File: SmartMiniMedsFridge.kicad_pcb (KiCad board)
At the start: 2 copper layers, 138 x 40 mm, 48 parts, among them J1 USB_C_Receptacle_USB2.0, J2 XHB-6AW, J3 Qwiic I2C, J4 Stemma I2C, U1 AMS1117-3.3, U2 ESP32-S3-WROOM-1, U3 LMV321, U4 MPR121QR2, U5 SSD1306

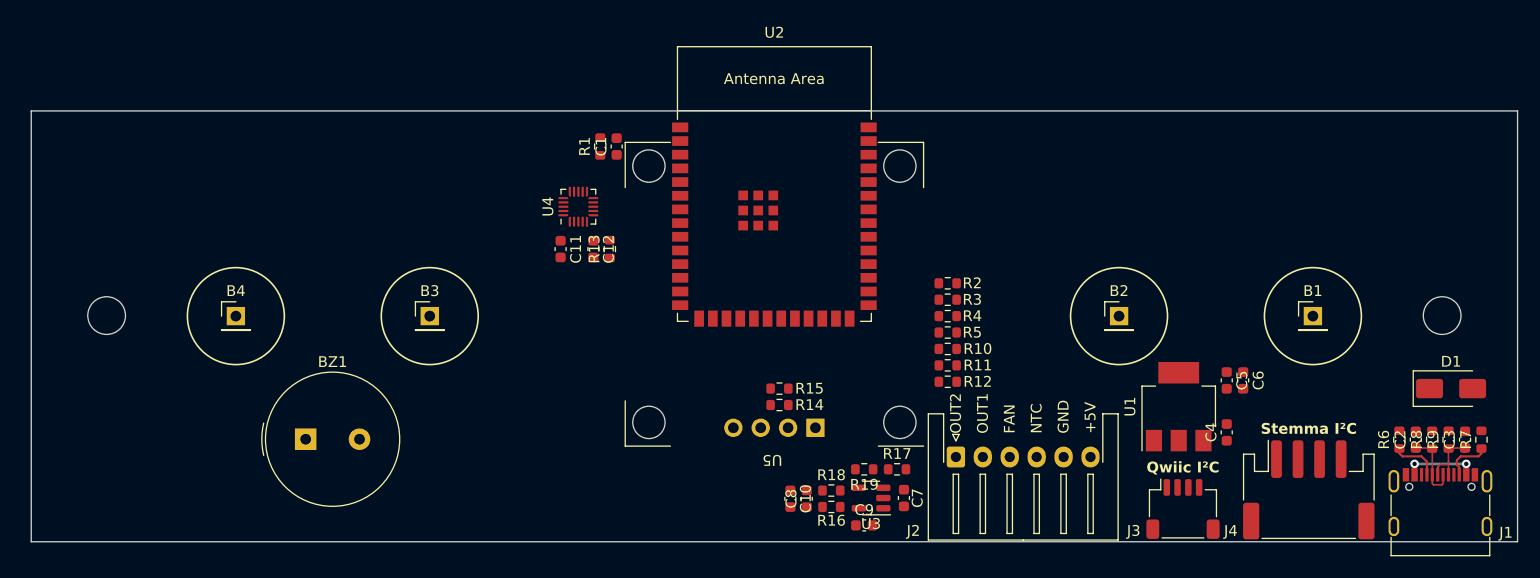
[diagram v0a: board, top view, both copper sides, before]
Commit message: pre re-arrangement because of collision with case
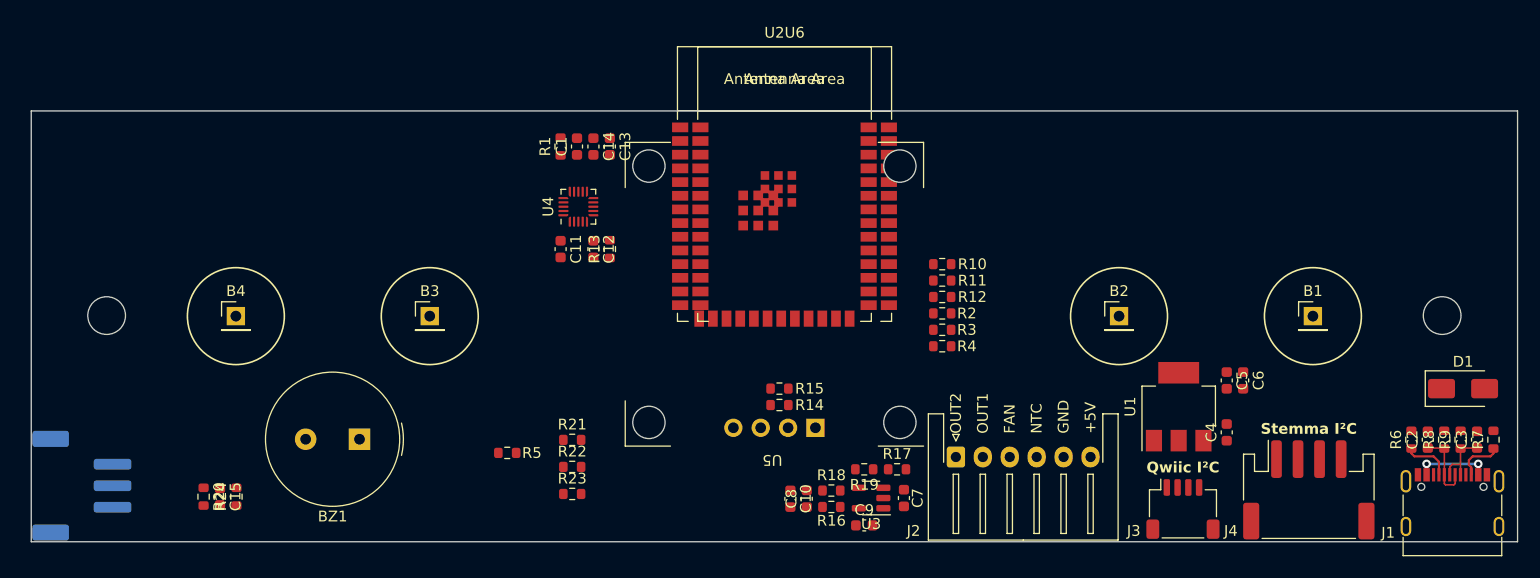
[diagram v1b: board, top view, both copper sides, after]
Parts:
- added C13: 22uF, Capacitor_SMD:C_0603_1608Metric, F.Cu at (117.2, 79.5)
- added C14: 100nF, Capacitor_SMD:C_0603_1608Metric, F.Cu at (115.7, 79.5)
- added C15: 100nF, Capacitor_SMD:C_0603_1608Metric, F.Cu at (81.0, 112.0)
- added J5: Door Sensor, Connector_JST:JST_PH_S3B-PH-SM4-TB_1x03-1MP_P2.00mm_Horizontal, B.Cu at (68.2, 111.0)
- added R20: 10k, Resistor_SMD:R_0603_1608Metric, F.Cu at (79.5, 112.0)
- added R21: 0R, Resistor_SMD:R_0603_1608Metric, F.Cu at (113.7, 106.7)
- added R22: 0R, Resistor_SMD:R_0603_1608Metric, F.Cu at (113.7, 109.2)
- added R23: 10k, Resistor_SMD:R_0603_1608Metric, F.Cu at (113.7, 111.8)
- added R24: 10k, Resistor_SMD:R_0603_1608Metric, F.Cu at (82.5, 112.0)
- added U6: ESP32-C6-WROOM-1, Espressif:ESP32-C6-WROOM-1, F.Cu at (134.4, 86.0)
- B1, B2, B3, B4: value Conn_01x01 -> Spring Contact
- U2: footprint PCM_Espressif:ESP32-S3-WROOM-1 -> Espressif:ESP32-S3-WROOM-1
- moved R5 42.4 mm to (107.7, 108.0)
- moved R11 7.89 mm to (148.1, 91.9)
- moved R12 7.89 mm to (148.1, 93.5)
- moved R10 7.89 mm to (148.1, 90.4)
- moved BZ1 5.00 mm to (94.0, 106.7), turned to 180 degrees
- moved C1 3.68 mm to (114.2, 79.5)
- moved R1 3.68 mm to (112.6, 79.5)
- moved R2 2.84 mm to (148.1, 95.0)
- moved R3 2.84 mm to (148.1, 96.5)
- moved R4 2.84 mm to (148.1, 98.0)
- moved C2 1.12 mm to (193.2, 106.7)
- moved C3 1.12 mm to (197.7, 106.7)
- moved D1 1.12 mm to (196.4, 102.0)
- moved J1 1.12 mm to (195.5, 113.7)
- moved R6 1.12 mm to (191.6, 106.7)
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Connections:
- J3 pad 3: SDA -> Ext_SDA
- J3 pad 4: SCL -> Ext_SCL
- J3 pad MP: (no net) -> unconnected-(J3-MountPin-PadMP)
- J4 pad 1: SCL -> Ext_SCL
- J4 pad 2: SDA -> Ext_SDA
- J4 pad MP: (no net) -> unconnected-(J4-MountPin-PadMP)
- R4 pad 1: Buzzer -> GPIO46
- R5 pad 1: C6_GPIO9 -> +3V3
- R5 pad 2: +3V3 -> Ext_SDA
- U2 pad 10: unconnected-(U2-GPIO17/U1TXD/ADC2_CH6-Pad10) -> /~{Touch_INT}
- U2 pad 11: /~{Touch_INT} -> /Door
- U2 pad 12: unconnected-(U2-GPIO8/TOUCH8/ADC1_CH7/SUBSPICS1-Pad12) -> Buzzer
- U2 pad 15: C6_GPIO9 -> unconnected-(U2-GPIO3/TOUCH3/ADC1_CH2-Pad15)
- U2 pad 16: Buzzer -> GPIO46
- U2 pad 17: SDA -> unconnected-(U2-GPIO9/TOUCH9/ADC1_CH8/FSPIHD/SUBSPIHD-Pad17)
- U2 pad 18: SCL -> unconnected-(U2-GPIO10/TOUCH10/ADC1_CH9/FSPICS0/FSPIIO4/SUBSPICS0-Pad18)
- U2 pad 19: /FAN_CPU -> unconnected-(U2-GPIO11/TOUCH11/ADC2_CH0/FSPID/FSPIIO5/SUBSPID-Pad19)
- U2 pad 20: /OUT1_CPU -> unconnected-(U2-GPIO12/TOUCH12/ADC2_CH1/FSPICLK/FSPIIO6/SUBSPICLK-Pad20)
- U2 pad 21: /OUT2_CPU -> unconnected-(U2-GPIO13/TOUCH13/ADC2_CH2/FSPIQ/FSPIIO7/SUBSPIQ-Pad21)
- U2 pad 28: unconnected-(U2-SPIIO6/GPIO35/FSPID/SUBSPID-Pad28) -> /OUT2_CPU
- U2 pad 29: unconnected-(U2-SPIIO7/GPIO36/FSPICLK/SUBSPICLK-Pad29) -> /OUT1_CPU
- U2 pad 30: unconnected-(U2-SPIDQS/GPIO37/FSPIQ/SUBSPIQ-Pad30) -> /FAN_CPU
- U2 pad 8: unconnected-(U2-GPIO15/U0RTS/ADC2_CH4/XTAL_32K_P-Pad8) -> SCL
- U2 pad 9: unconnected-(U2-GPIO16/U0CTS/ADC2_CH5/XTAL_32K_N-Pad9) -> SDA

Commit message: 1st production version
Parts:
- removed the U6 at (134.4, 86.0)
- added D2: LED_Small, LED_SMD:LED_0603_1608Metric, F.Cu at (149.2, 94.2)
- added D3: LED_Small, LED_SMD:LED_0603_1608Metric, F.Cu at (178.1, 86.4)
- added J6: UART, Connector_PinHeader_2.54mm:PinHeader_1x06_P2.54mm_Vertical, F.Cu at (161.0, 80.9)
- added R18: 1k, Resistor_SMD:R_0603_1608Metric, F.Cu at (144.0, 88.9)
- added R19: 1k, Resistor_SMD:R_0603_1608Metric, F.Cu at (178.1, 83.3)
- added R24: 100R, Resistor_SMD:R_0603_1608Metric, F.Cu at (144.0, 96.5)
- added REF**: OSHW-Logo2_9.8x8mm_SilkScreen, Symbol:OSHW-Logo2_9.8x8mm_SilkScreen, F.Cu at (69.6, 88.0)
- added SW1: Reset, Button_Switch_SMD:SW_Push_1P1T-SH_NO_CK_KMR2xxG, F.Cu at (103.5, 79.5)
- J1: footprint Connector_USB:USB_C_Receptacle_G-Switch_GT-USB-7010ASV -> Connector_USB:USB_C_Receptacle_G-Switch_GT-USB-7051x
- J5: moved to F.Cu
- moved D1 93.4 mm to (103.6, 112.4), turned to -90 degrees
- moved C5 89.5 mm to (108.2, 107.7)
- moved R11 86.5 mm to (109.7, 107.7)
- moved J1 85.0 mm to (110.5, 112.4)
- moved R6 85.0 mm to (114.3, 107.7)
- moved R5 85.0 mm to (106.7, 107.7)
- moved R10 83.4 mm to (111.3, 107.7)
- moved C4 80.4 mm to (112.8, 107.7)
- moved R12 51.0 mm to (158.4, 102.6), turned to 180 degrees
- moved R13 45.3 mm to (158.4, 104.1), turned to 180 degrees
- moved R15 41.9 mm to (155.3, 104.1)
- moved R14 41.8 mm to (155.3, 102.6)
- moved R16 30.6 mm to (153.8, 86.9)
- moved C10 29.3 mm to (151.5, 87.7)
- moved C11 29.3 mm to (156.8, 90.2)
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- renumbered C13 to C1, C8 to C10, C9 to C11, C15 to C12, C10 to C13, C11 to C14, C12 to C15, C14 to C2, C1 to C3, C2 to C4, C3 to C5, C7 to C6, C4 to C7, C5 to C8, C6 to C9, R2 to R1, R8 to R10, R9 to R11, R5 to R12, R23 to R13, R21 to R14, R22 to R15, R18 to R17, R3 to R2, R17 to R21, R24 to R22, R19 to R23, R14 to R25, R15 to R26, R13 to R27, R4 to R3, R1 to R4, R6 to R5, R7 to R6, R10 to R7, R11 to R8, R12 to R9, U3 to U2, U2 to U3, U4 to U5, U5 to U6
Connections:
- J1 pad S1: unconnected-(J1-SHIELD-PadS1) -> GND
- J3 pad MP: unconnected-(J3-MountPin-PadMP) -> GND
- J4 pad MP: unconnected-(J4-MountPin-PadMP) -> GND
- J5 pad MP: unconnected-(J5-MountPin-PadMP) -> GND
- U3 pad 24: unconnected-(U2-GPIO47/SPICLK_P/SUBSPICLK_P_DIFF-Pad24) -> Ext_SDA
- U3 pad 25: unconnected-(U2-GPIO48/SPICLK_N/SUBSPICLK_N_DIFF-Pad25) -> Ext_SCL
- U3 pad 31: unconnected-(U2-GPIO38/FSPIWP/SUBSPIWP-Pad31) -> /GPIO38
- U3 pad 32: unconnected-(U2-MTCK/GPIO39/CLK_OUT3/SUBSPICS1-Pad32) -> /GPIO39
- U3 pad 33: unconnected-(U2-MTDO/GPIO40/CLK_OUT2-Pad33) -> /GPIO40
- U3 pad 35: unconnected-(U2-MTMS/GPIO42-Pad35) -> /GPIO42
- U3 pad 8: SCL -> SDA
- U3 pad 9: SDA -> SCL
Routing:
- net +3V3: track 0.00 -> 249.9 mm, vias 0 -> 7
- net +5V: track 0.00 -> 141.3 mm, vias 0 -> 5
- net Touch0: track 0.00 -> 86.9 mm, vias 0 -> 2
- net SDA: track 0.00 -> 74.9 mm, vias 0 -> 3
- net SCL: track 0.00 -> 73.4 mm, vias 0 -> 3
- net Touch1: track 0.00 -> 68.7 mm, vias 0 -> 2
- net ~{RESET}: track 0.00 -> 67.9 mm, vias 0 -> 4
- net Touch3: track 0.00 -> 54.2 mm, vias 0 -> 1
- net /Door: track 0.00 -> 53.9 mm
- net Ext_SDA: track 0.00 -> 43.3 mm
- net ADC_Supply: track 0.00 -> 41.5 mm, vias 0 -> 2
- net /FAN: track 0.00 -> 39.9 mm
- net /OUT1: track 0.00 -> 37.5 mm
- net Touch2: track 0.00 -> 37.2 mm, vias 0 -> 2
- net Buzzer: track 0.00 -> 36.9 mm
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- added copper zone on B.Cu, net GND
- added copper zone on F.Cu, net GND
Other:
- board text added: "+3V3"
- board text added: "3V3"
- board text added: "BOOT"
- board text added: "Door Sensor"
- board text added: "JLCJLCJLCJLC"
- board text added: "RXD"
- board text added: "Reset"
- board text added: "S3:GPIO18 C6:GPIO10"
- board text added: "Smart Meds Mini Fridge EvilScientress"
- board text added: "TXD"
- board text added: "UART"
- board text added: "rev 1"
- board text added: "~{RESET}"
